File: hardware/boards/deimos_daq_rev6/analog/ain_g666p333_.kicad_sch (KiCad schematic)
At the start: 6 parts, among them IC36001 INA826AIDR

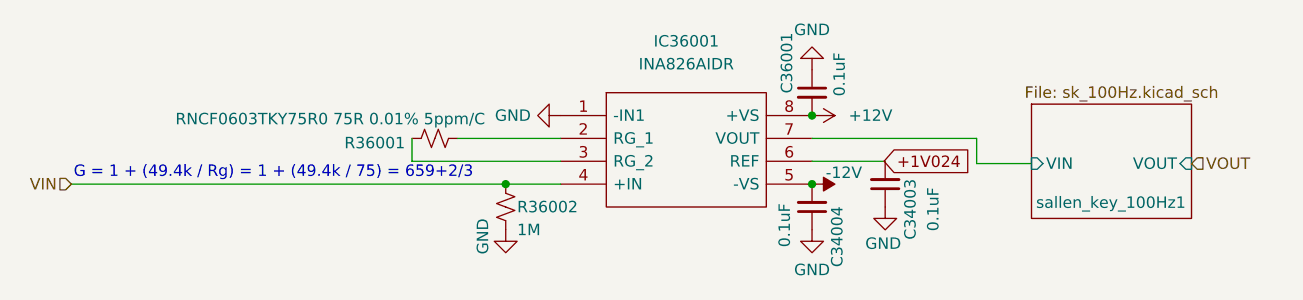
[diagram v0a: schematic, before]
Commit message: exclude testpoints from BOM
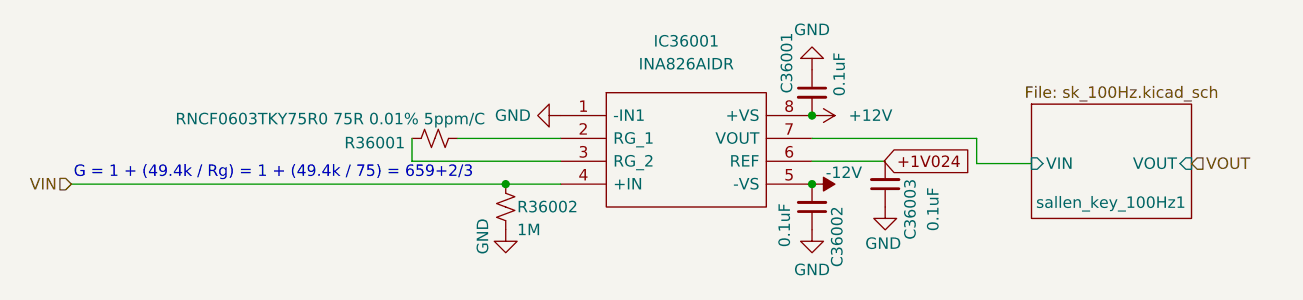
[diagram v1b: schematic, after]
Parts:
- renumbered C34004 to C36002, C34003 to C36003
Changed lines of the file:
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@@
 		(dnp no)
 		(fields_autoplaced yes)
-		(property "Reference" "#PWR34009"
+		(property "Reference" "#PWR315"
 			(at 158.496 119.634 0)
 			(effects
@@
 		)
 		(instances
+			(project "analog_i"
+				(path "/5a60c4b1-b6cb-416e-8883-8291fa089b87/c2baf18d-2b19-4edb-98b3-535275ee271f/ed60502d-2e6d-4293-85f2-5e967a3c42d8"
+					(reference "#PWR315")
+					(unit 1)
+				)
+			)
 			(project "analog_frontend_panel"
 				(path "/c241d083-1323-4b4a-a540-956d0afb7b72/ed60502d-2e6d-4293-85f2-5e967a3c42d8"
@@
 		(on_board yes)
 		(dnp no)
-		(property "Reference" "C34004"
+		(property "Reference" "C36002"
 			(at 161.29 114.046 90)
 			(effects
@@
 		)
 		(instances
+			(project "analog_i"
+				(path "/5a60c4b1-b6cb-416e-8883-8291fa089b87/c2baf18d-2b19-4edb-98b3-535275ee271f/ed60502d-2e6d-4293-85f2-5e967a3c42d8"
+					(reference "C36002")
+					(unit 1)
+				)
+			)
 			(project "analog_frontend_panel"
 				(path "/c241d083-1323-4b4a-a540-956d0afb7b72/ed60502d-2e6d-4293-85f2-5e967a3c42d8"
@@
 		(dnp no)
 		(fields_autoplaced yes)
-		(property "Reference" "#PWR34007"
+		(property "Reference" "#PWR310"
 			(at 154.686 100.584 0)
 			(effects
@@
 		)
 		(instances
+			(project "analog_i"
+				(path "/5a60c4b1-b6cb-416e-8883-8291fa089b87/c2baf18d-2b19-4edb-98b3-535275ee271f/ed60502d-2e6d-4293-85f2-5e967a3c42d8"
+					(reference "#PWR310")
+					(unit 1)
+				)
+			)
 			(project ""
 				(path "/c241d083-1323-4b4a-a540-956d0afb7b72/ed60502d-2e6d-4293-85f2-5e967a3c42d8"
@@
 		(on_board yes)
 		(dnp no)
-		(property "Reference" "#PWR34008"
+		(property "Reference" "#PWR311"
 			(at 154.686 108.204 0)
 			(effects
@@
 		)
 		(instances
+			(project "analog_i"
+				(path "/5a60c4b1-b6cb-416e-8883-8291fa089b87/c2baf18d-2b19-4edb-98b3-535275ee271f/ed60502d-2e6d-4293-85f2-5e967a3c42d8"
+					(reference "#PWR311")
+					(unit 1)
+				)
+			)
 			(project ""
 				(path "/c241d083-1323-4b4a-a540-956d0afb7b72/ed60502d-2e6d-4293-85f2-5e967a3c42d8"
@@
 		(on_board yes)
 		(dnp no)
-		(property "Reference" "#PWR34006"
+		(property "Reference" "#PWR314"
 			(at 166.624 117.094 0)
 			(effects
@@
 		)
 		(instances
+			(project "analog_i"
+				(path "/5a60c4b1-b6cb-416e-8883-8291fa089b87/c2baf18d-2b19-4edb-98b3-535275ee271f/ed60502d-2e6d-4293-85f2-5e967a3c42d8"
+					(reference "#PWR314")
+					(unit 1)
+				)
+			)
 			(project "analog_frontend_panel"
 				(path "/c241d083-1323-4b4a-a540-956d0afb7b72/ed60502d-2e6d-4293-85f2-5e967a3c42d8"
@@
 		(on_board yes)
 		(dnp no)
-		(property "Reference" "C34003"
+		(property "Reference" "C36003"
 			(at 169.418 110.998 90)
 			(effects
@@
 		)
 		(instances
+			(project "analog_i"
+				(path "/5a60c4b1-b6cb-416e-8883-8291fa089b87/c2baf18d-2b19-4edb-98b3-535275ee271f/ed60502d-2e6d-4293-85f2-5e967a3c42d8"
+					(reference "C36003")
+					(unit 1)
+				)
+			)
 			(project "analog_frontend_panel"
 				(path "/c241d083-1323-4b4a-a540-956d0afb7b72/ed60502d-2e6d-4293-85f2-5e967a3c42d8"
